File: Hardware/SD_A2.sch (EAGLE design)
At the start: 25 parts, among them IC1 74LS245N, IC2 LM317, IC4 XC9572XL, IC5 28C64ASO

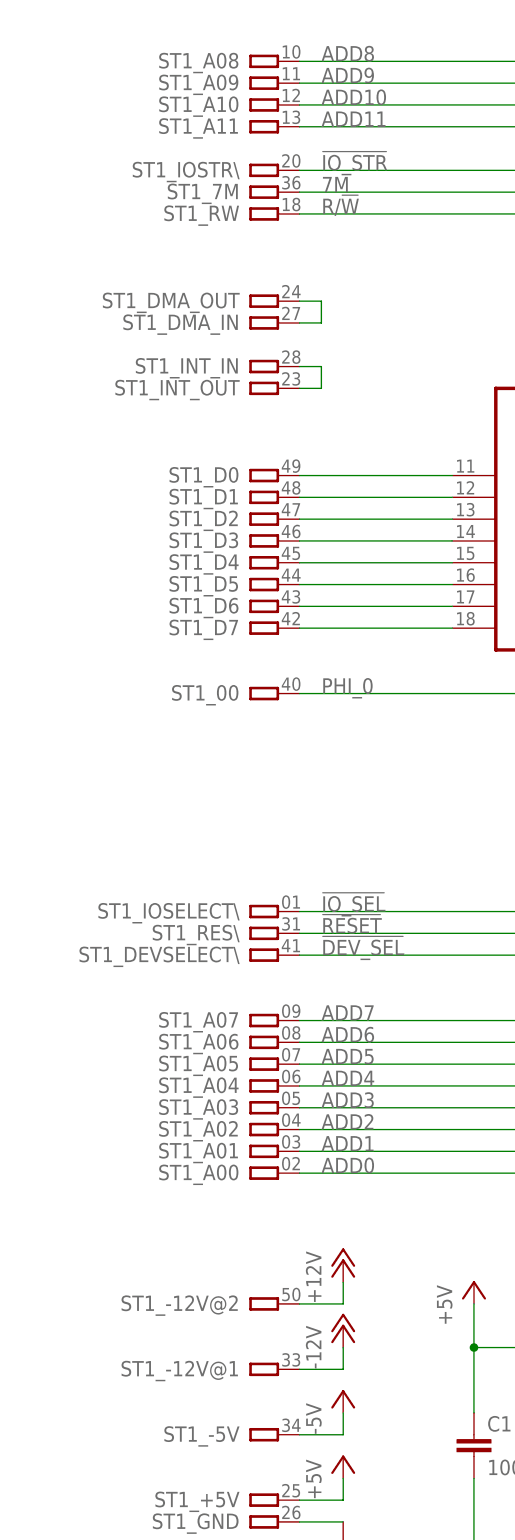
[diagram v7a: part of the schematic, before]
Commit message: Rename in AII connector
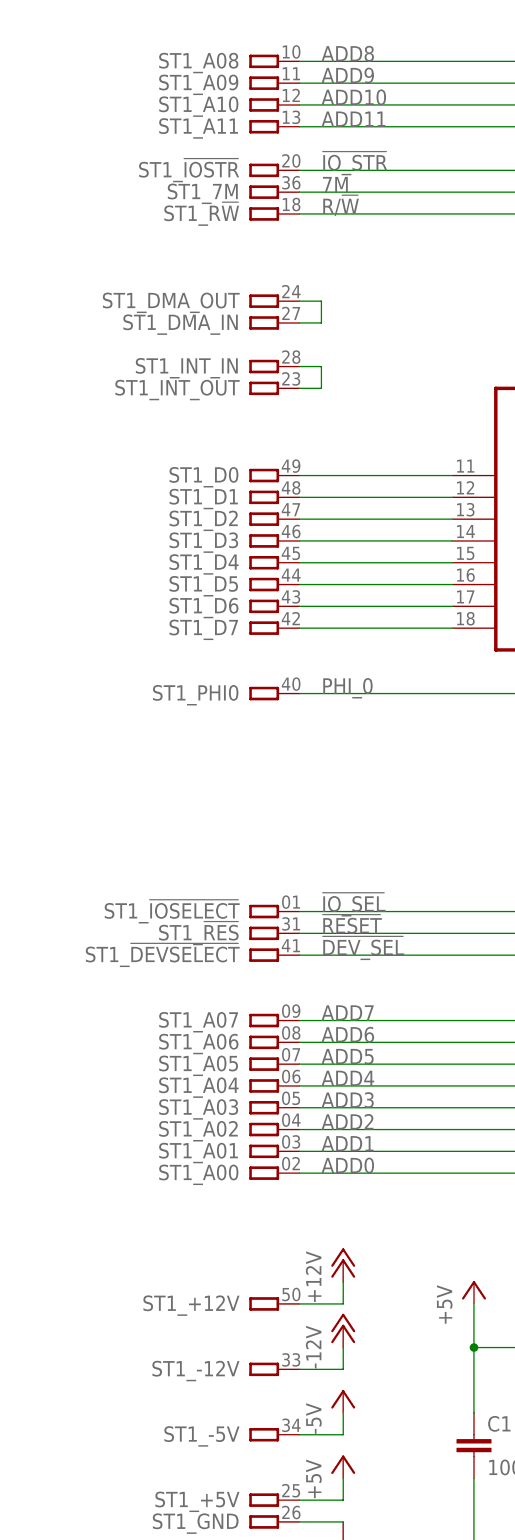
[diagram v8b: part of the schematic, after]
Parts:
- ST1: value (none) -> A2-50PINSLOT1-3
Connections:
- net !DEV_SEL: now also ST1_!DEVSELECT.P; no longer ST1_DEVSELECT\.P
- net !IO_SEL: now also ST1_!IOSELECT.P; no longer ST1_IOSELECT\.P
- net !IO_STR: now also ST1_!IOSTR.P; no longer ST1_IOSTR\.P
- net !RESET: now also ST1_!RES.P; no longer ST1_RES\.P
- net +12V: now also ST1_+12V.P; no longer ST1_-12V@2.P
- net -12V: now also ST1_-12V.P; no longer ST1_-12V@1.P
- net PHI_0: now also ST1_PHI0.P; no longer ST1_00.P
- net R/!W: now also ST1_R!W.P; no longer ST1_RW.P
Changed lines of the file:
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@@
 </plain>
 <instances>
-<instance part="ST1" gate="_-12V@2" x="73.66" y="35.56" rot="R180"/>
+<instance part="ST1" gate="_+12V" x="73.66" y="35.56" rot="R180"/>
 <instance part="ST1" gate="_D0" x="73.66" y="132.08" rot="R180"/>
 <instance part="ST1" gate="_D1" x="73.66" y="129.54" rot="R180"/>
@@
 <instance part="ST1" gate="_D6" x="73.66" y="116.84" rot="R180"/>
 <instance part="ST1" gate="_D7" x="73.66" y="114.3" rot="R180"/>
-<instance part="ST1" gate="_DEVSELECT\" x="73.66" y="76.2" rot="R180"/>
-<instance part="ST1" gate="_00" x="73.66" y="106.68" rot="R180"/>
+<instance part="ST1" gate="_!DEVSELECT" x="73.66" y="76.2" rot="R180"/>
+<instance part="ST1" gate="_PHI0" x="73.66" y="106.68" rot="R180"/>
 <instance part="ST1" gate="_7M" x="73.66" y="165.1" rot="R180"/>
 <instance part="ST1" gate="_-5V" x="73.66" y="20.32" rot="R180"/>
-<instance part="ST1" gate="_-12V@1" x="73.66" y="27.94" rot="R180"/>
-<instance part="ST1" gate="_RES\" x="73.66" y="78.74" rot="R180"/>
+<instance part="ST1" gate="_-12V" x="73.66" y="27.94" rot="R180"/>
+<instance part="ST1" gate="_!RES" x="73.66" y="78.74" rot="R180"/>
 <instance part="ST1" gate="_INT_IN" x="73.66" y="144.78" rot="R180"/>
 <instance part="ST1" gate="_DMA_IN" x="73.66" y="149.86" rot="R180"/>
 <instance part="ST1" gate="_GND" x="73.66" y="10.16" rot="R180"/>
-<instance part="ST1" gate="_IOSELECT\" x="73.66" y="81.28" rot="R180"/>
+<instance part="ST1" gate="_!IOSELECT" x="73.66" y="81.28" rot="R180"/>
 <instance part="ST1" gate="_A00" x="73.66" y="50.8" rot="R180"/>
 <instance part="ST1" gate="_A01" x="73.66" y="53.34" rot="R180"/>
@@
 <instance part="ST1" gate="_A10" x="73.66" y="175.26" rot="R180"/>
 <instance part="ST1" gate="_A11" x="73.66" y="172.72" rot="R180"/>
-<instance part="ST1" gate="_RW" x="73.66" y="162.56" rot="R180"/>
-<instance part="ST1" gate="_IOSTR\" x="73.66" y="167.64" rot="R180"/>
+<instance part="ST1" gate="_R!W" x="73.66" y="162.56" rot="R180"/>
+<instance part="ST1" gate="_!IOSTR" x="73.66" y="167.64" rot="R180"/>
 <instance part="ST1" gate="_INT_OUT" x="73.66" y="142.24" rot="R180"/>
 <instance part="ST1" gate="_DMA_OUT" x="73.66" y="152.4" rot="R180"/>
@@
 <pinref part="IC1" gate="A" pin="DIR"/>
 <label x="124.46" y="137.16" size="1.778" layer="95"/>
-<pinref part="ST1" gate="_RW" pin="P"/>
+<pinref part="ST1" gate="_R!W" pin="P"/>
 <wire x1="76.2" y1="162.56" x2="132.08" y2="162.56" width="0.1524" layer="91"/>
 <wire x1="132.08" y1="162.56" x2="167.64" y2="162.56" width="0.1524" layer="91"/>
@@
 <net name="PHI_0" class="0">
 <segment>
-<pinref part="ST1" gate="_00" pin="P"/>
+<pinref part="ST1" gate="_PHI0" pin="P"/>
 <wire x1="76.2" y1="106.68" x2="162.56" y2="106.68" width="0.1524" layer="91"/>
 <label x="78.74" y="106.68" size="1.778" layer="95"/>
@@
 <net name="!IO_STR" class="0">
 <segment>
-<pinref part="ST1" gate="_IOSTR\" pin="P"/>
+<pinref part="ST1" gate="_!IOSTR" pin="P"/>
 <wire x1="195.58" y1="167.64" x2="76.2" y2="167.64" width="0.1524" layer="91"/>
 <label x="78.74" y="167.64" size="1.778" layer="95"/>
@@
 <wire x1="208.28" y1="76.2" x2="208.28" y2="93.98" width="0.1524" layer="91"/>
 <wire x1="208.28" y1="76.2" x2="76.2" y2="76.2" width="0.1524" layer="91"/>
-<pinref part="ST1" gate="_DEVSELECT\" pin="P"/>
+<pinref part="ST1" gate="_!DEVSELECT" pin="P"/>
 </segment>
 </net>
@@
 <wire x1="205.74" y1="78.74" x2="205.74" y2="93.98" width="0.1524" layer="91"/>
 <label x="78.74" y="78.74" size="1.778" layer="95"/>
-<pinref part="ST1" gate="_RES\" pin="P"/>
+<pinref part="ST1" gate="_!RES" pin="P"/>
 </segment>
 </net>
@@
 <pinref part="IC4" gate="G$1" pin="FB03/09"/>
 <wire x1="198.12" y1="93.98" x2="198.12" y2="81.28" width="0.1524" layer="91"/>
-<pinref part="ST1" gate="_IOSELECT\" pin="P"/>
+<pinref part="ST1" gate="_!IOSELECT" pin="P"/>
 <wire x1="198.12" y1="81.28" x2="76.2" y2="81.28" width="0.1524" layer="91"/>
 <label x="78.74" y="81.28" size="1.778" layer="95"/>
@@
 <net name="+12V" class="0">
 <segment>
-<pinref part="ST1" gate="_-12V@2" pin="P"/>
+<pinref part="ST1" gate="_+12V" pin="P"/>
 <pinref part="P+6" gate="1" pin="+12V"/>
 <wire x1="76.2" y1="35.56" x2="81.28" y2="35.56" width="0.1524" layer="91"/>
@@
 <net name="-12V" class="0">
 <segment>
-<pinref part="ST1" gate="_-12V@1" pin="P"/>
+<pinref part="ST1" gate="_-12V" pin="P"/>
 <pinref part="P-2" gate="1" pin="-12V"/>
 <wire x1="76.2" y1="27.94" x2="81.28" y2="27.94" width="0.1524" layer="91"/>
